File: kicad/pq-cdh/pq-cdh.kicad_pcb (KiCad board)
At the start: 4 copper layers, 43 x 43 mm, 35 parts, among them IC1 STM32L496RGT3, IC2 IS25LP128F-JBLA3, J1 Conn_01x04, J2 Conn_01x16, J3 Conn_01x04, J4 Conn_01x04, J5 Conn_01x16, J6 Conn_01x04, J7 Conn_02x06_Odd_Even, J8 Conn_01x04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

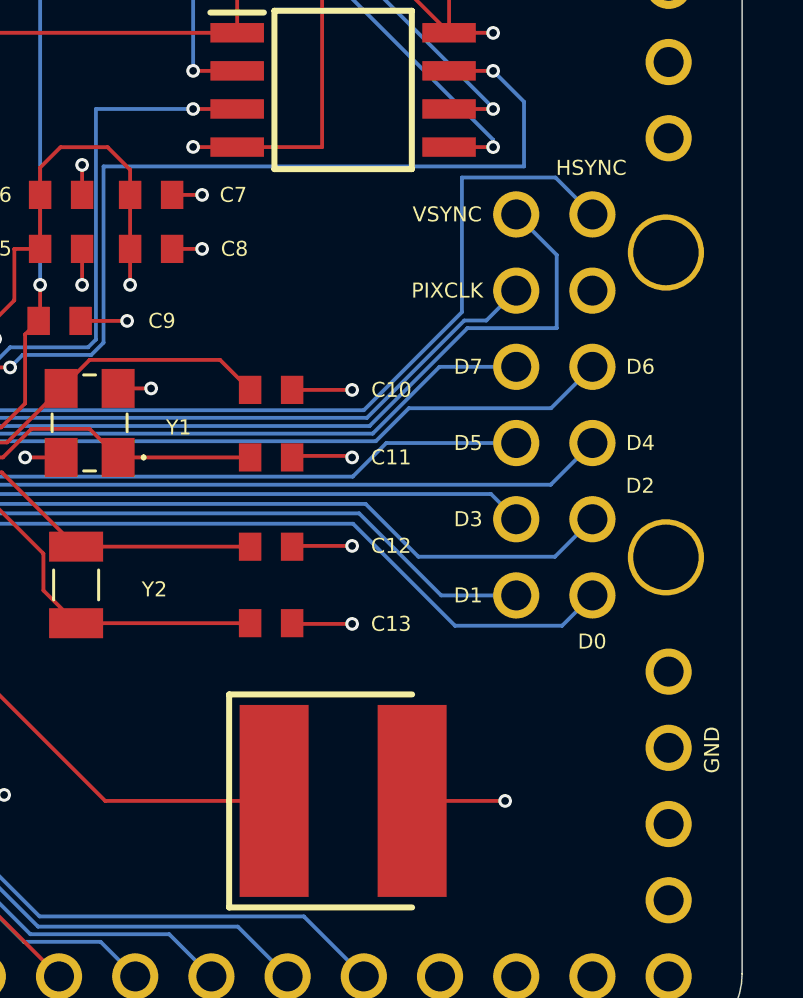
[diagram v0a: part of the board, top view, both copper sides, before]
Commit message: MountingHoles_adjustment
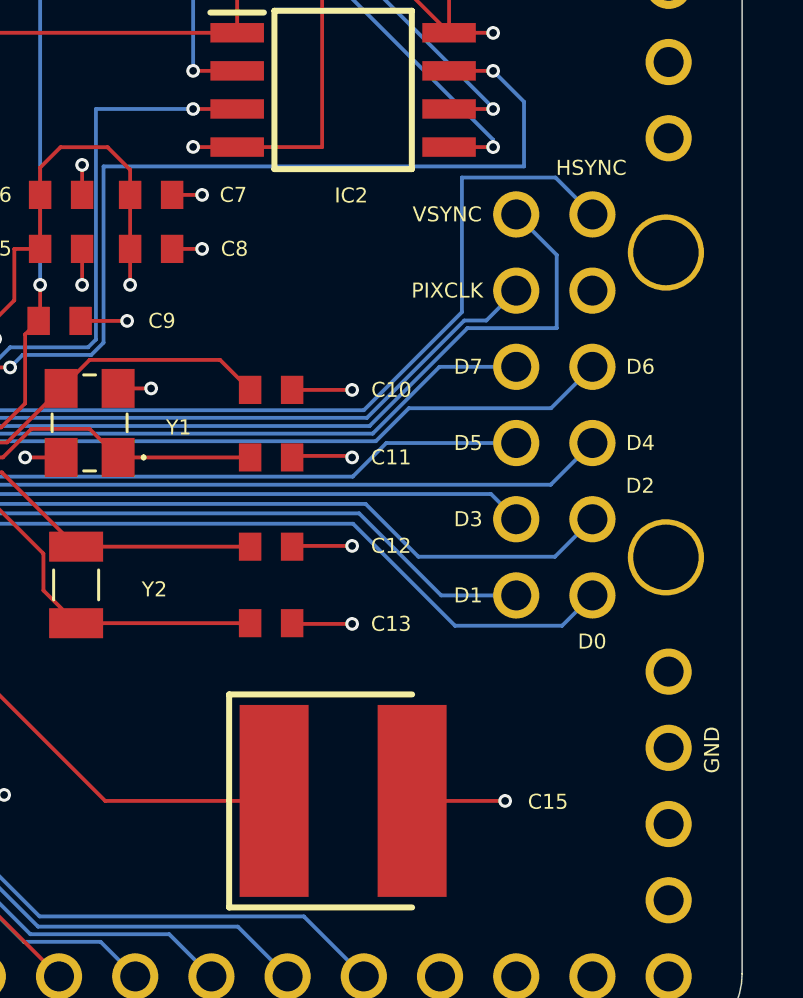
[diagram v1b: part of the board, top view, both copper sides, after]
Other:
- board text added: "C15"
- board text added: "IC2"
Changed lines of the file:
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@@
+    (effects (font (size 0.5 0.5) (thickness 0.1)))
+  )
+  (gr_text "C15" (at 170.03 121.23) (layer "F.SilkS")
     (effects (font (size 0.5 0.5) (thickness 0.1)))
   )
@@
     (effects (font (size 0.5 0.5) (thickness 0.1)))
   )
+  (gr_text "IC2" (at 163.47 101.02) (layer "F.SilkS")
+    (effects (font (size 0.5 0.5) (thickness 0.1)))
+  )

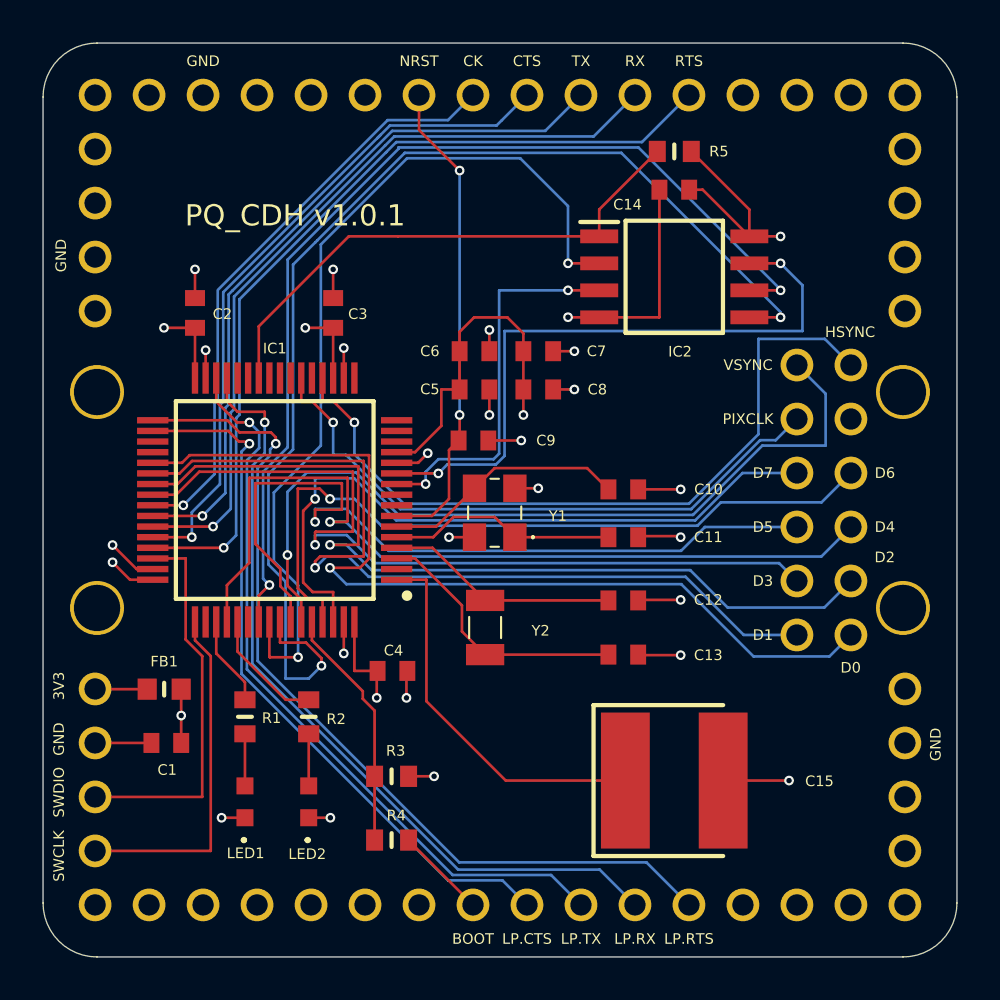
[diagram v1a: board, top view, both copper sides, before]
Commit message: Review_update_mountingHole_Clearance
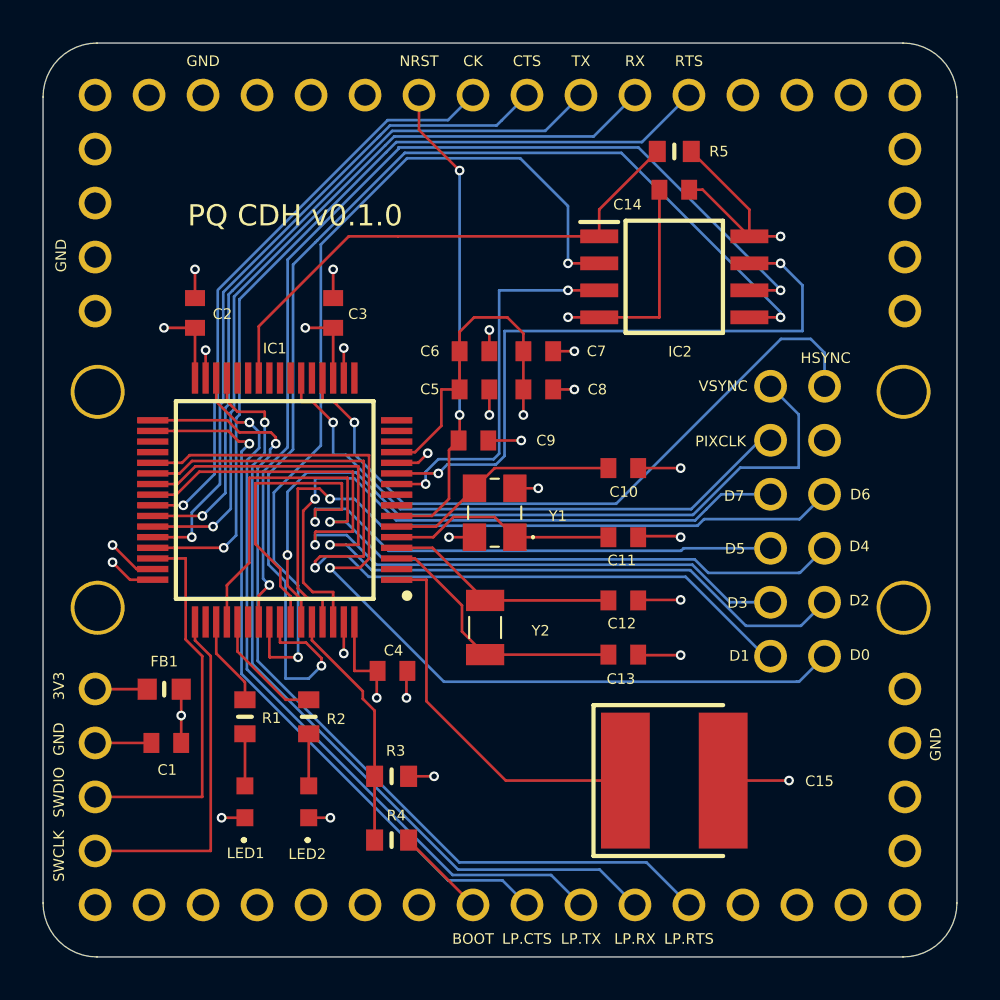
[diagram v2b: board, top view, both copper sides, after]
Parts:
- moved J7 1.59 mm to (169.0, 109.0)
- moved C10 1.00 mm to (160.8, 106.5)
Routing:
- net /DCMI_HSYNC: track 35.2 -> 32.7 mm
- net /DCMI_VSYNC: track 38.6 -> 36.9 mm
- net /DCMI_D7: track 32.5 -> 30.9 mm
- net /DCMI_D5: track 38.9 -> 37.3 mm
- net /DCMI_D6: track 34.9 -> 33.3 mm
- net /DCMI_D4: track 40.5 -> 39.5 mm
- net /DCMI_D2: track 41.3 -> 40.3 mm
- net /DCMI_D1: track 41.8 -> 40.9 mm
- net /DCMI_D3: track 39.1 -> 38.2 mm
- net /DCMI_D0: track 43.9 -> 43.2 mm
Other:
- board text added: "PQ CDH v0.1.0"
- board text removed: "PQ_CDH v1.0.1"
